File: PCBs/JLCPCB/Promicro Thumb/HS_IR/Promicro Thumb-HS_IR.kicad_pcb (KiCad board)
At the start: 2 copper layers, 100.7 x 63.3 mm, 64 parts, among them J1 USB_C_Receptacle_USB2.0, J2 Conn_01x04_Socket, Q1 PT26-51B/TR8, Q2 PT26-51B/TR8, SW1 TMAG5231H1DQDBZR, SW2 TMAG5231H1DQDBZR, SW3 TMAG5231H1DQDBZR, SW4 TMAG5231H1DQDBZR, SW5 TMAG5231H1DQDBZR, SW6 TMAG5231H1DQDBZR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

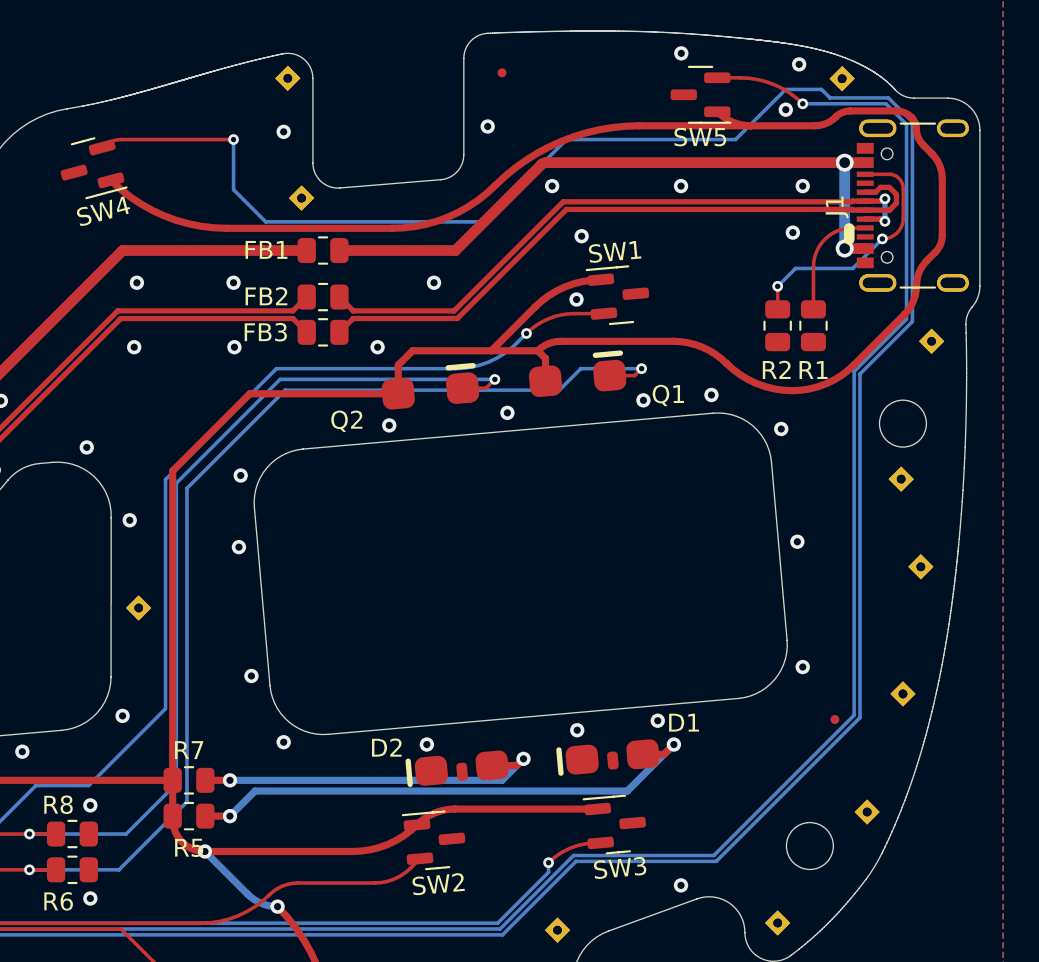
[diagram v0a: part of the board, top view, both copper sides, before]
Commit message: Smaller 3V3 tracks
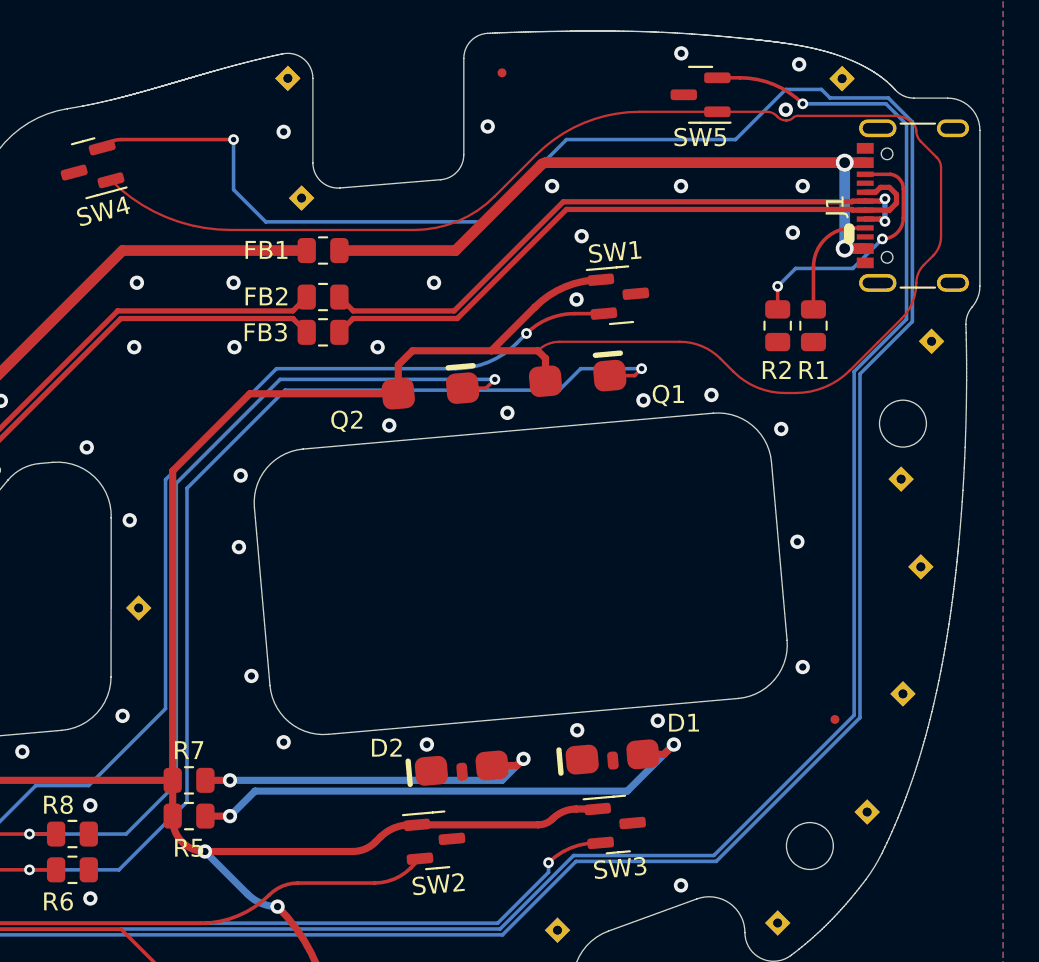
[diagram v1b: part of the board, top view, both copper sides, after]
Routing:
- net +3V3: track 380.0 -> 378.6 mm
